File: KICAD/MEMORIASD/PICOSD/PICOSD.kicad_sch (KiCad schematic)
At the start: 2 parts, among them J1 SD_Card, U1 Pico

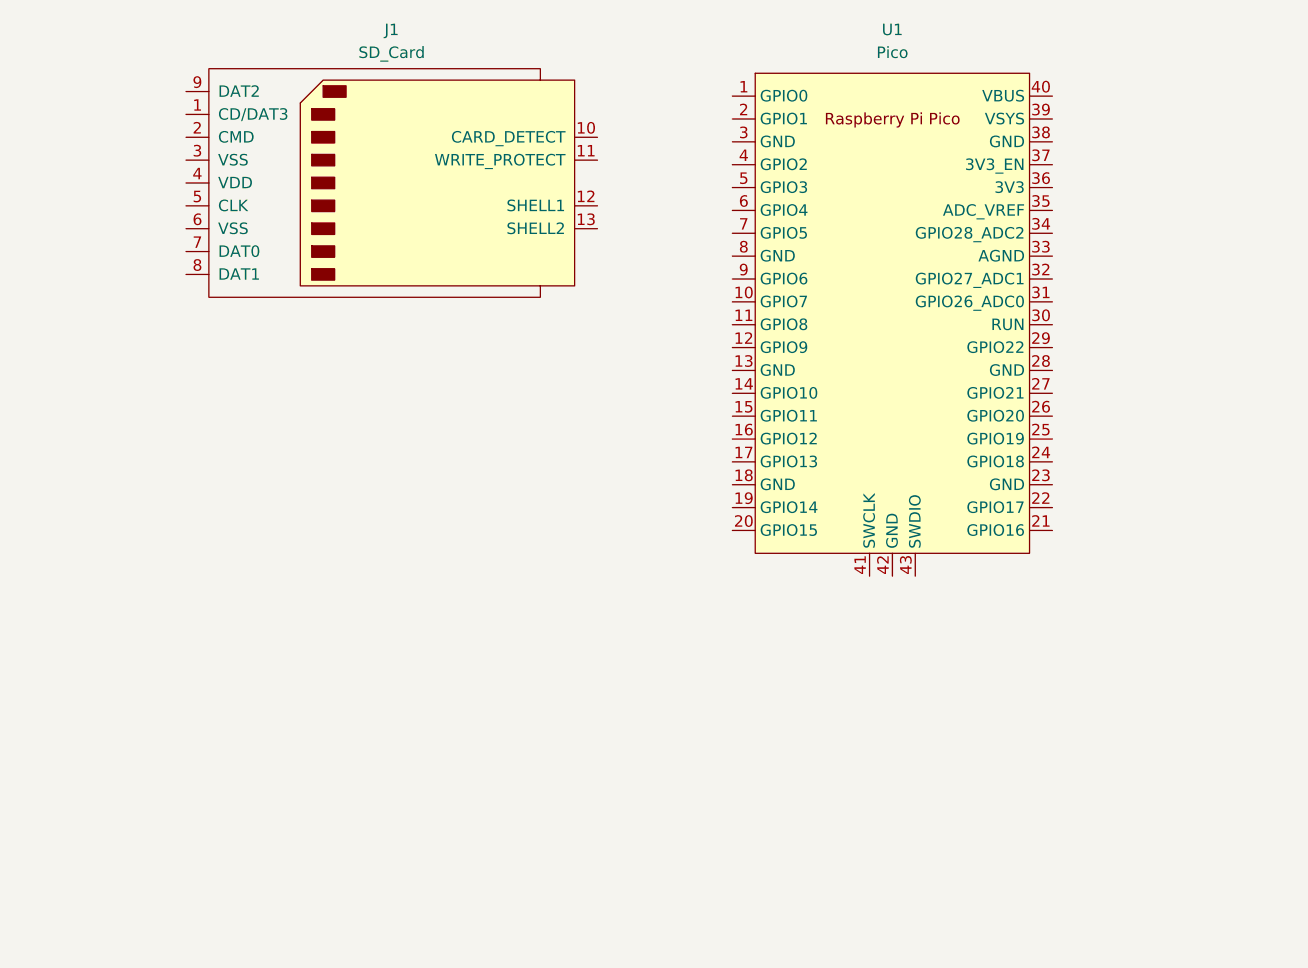
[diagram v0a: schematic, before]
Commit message: Adicion en Informe, Adicion de Diagrama de tareas y conexiones, Ajuste de los K del PID, Adicion de modulo SD en KICAD
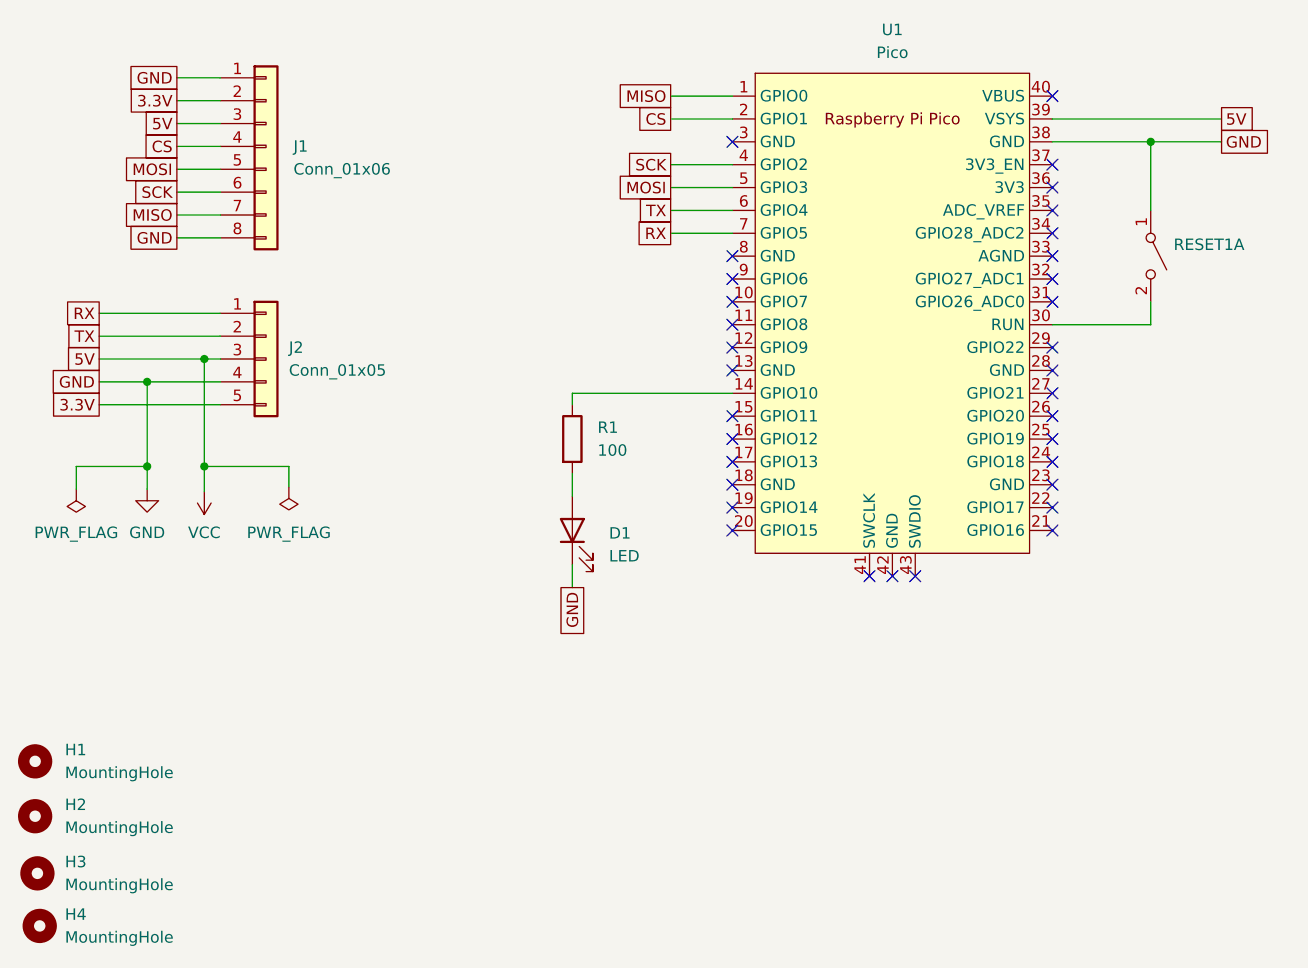
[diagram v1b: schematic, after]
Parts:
- removed J1: SD_Card, symbol Connector:SD_Card
- added D1: LED, LED_THT:LED_D5.0mm, symbol Device:LED
- added H1, H2, H3, H4: MountingHole, MountingHole:MountingHole_4mm, symbol Mechanical:MountingHole
- added J1: Conn_01x06, Connector_PinHeader_2.54mm:PinHeader_1x08_P2.54mm_Vertical, symbol Connector_Generic:Conn_01x08
- added J2: Conn_01x05, Connector_PinHeader_2.54mm:PinHeader_1x05_P2.54mm_Vertical, symbol Connector_Generic:Conn_01x05
- added R1: 100, Resistor_THT:R_Axial_DIN0204_L3.6mm_D1.6mm_P7.62mm_Horizontal, symbol Device:R
- added RESET1: SW_DPST_x2, Button_Switch_THT:SW_Push_2P1T_Toggle_CK_PVA1xxH4xxxxxxV2, symbol Switch:SW_DPST_x2
- U1: footprint RPi_Pico:RPi_Pico_SMD_TH -> MCU_RaspberryPi_and_Boards:RPi_Pico_SMD_TH
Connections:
- net MISO: now reaches U1.1 (GPIO0)
- net MISO: now also J1.7 (Pin_7)
- net at U1.14 (GPIO10): now also R1.1
- net CS: now reaches U1.2 (GPIO1)
- net CS: now also J1.4 (Pin_4)
- net at U1.30 (RUN): now also RESET1.2 (B)
- net GND: now reaches U1.38 (GND)
- net GND: now also D1.1 (K), J1.1 (Pin_1), J1.8 (Pin_8), J2.4 (Pin_4), RESET1.1 (A)
- net VCC: now reaches U1.39 (VSYS)
- net VCC: now also J1.3 (Pin_3), J2.3 (Pin_3)
- net SCK: now reaches U1.4 (GPIO2)
- net SCK: now also J1.6 (Pin_6)
- net MOSI: now reaches U1.5 (GPIO3)
- net MOSI: now also J1.5 (Pin_5)
- net TX: now reaches U1.6 (GPIO4)
- net TX: now also J2.2 (Pin_2)
- net RX: now reaches U1.7 (GPIO5)
- net RX: now also J2.1 (Pin_1)
- new net: D1.2 (A), R1.2
- new net 3.3V: J1.2 (Pin_2), J2.5 (Pin_5)
- no-connect marks 0 -> 33
